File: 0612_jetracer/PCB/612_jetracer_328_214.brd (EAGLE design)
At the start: 86.7 x 51.7 mm, 90 parts, among them IC2 JETSON_NANO_NOBORDER, IC3 MULTIPLEXERSMC74HC157A, M1 MOSFET-N_FDN335N, M2 MOSFET-N_FDN335N, M3 MOSFET-N_FDN335N, M4 MOSFET-N_FDN335N, M5 MOSFET-N_FDN335N, M6 MOSFET-N_FDN335N, Q1 MOSFET-N_FDN335N, Q2 MOSFET-N_FDN335N, X2 16MHz

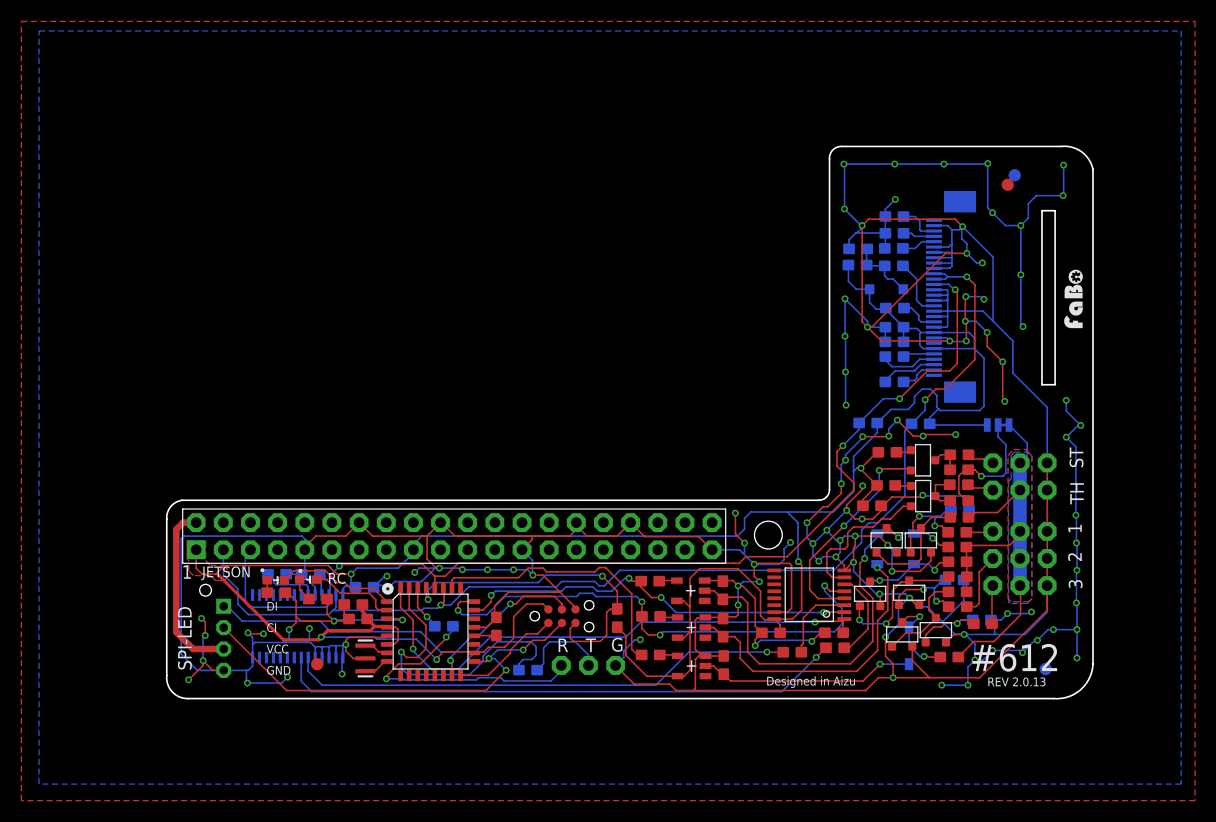
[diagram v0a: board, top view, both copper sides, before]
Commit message: #612 JetRacer ファイルリネーム,シルク追加位置修正、GNDビア追加
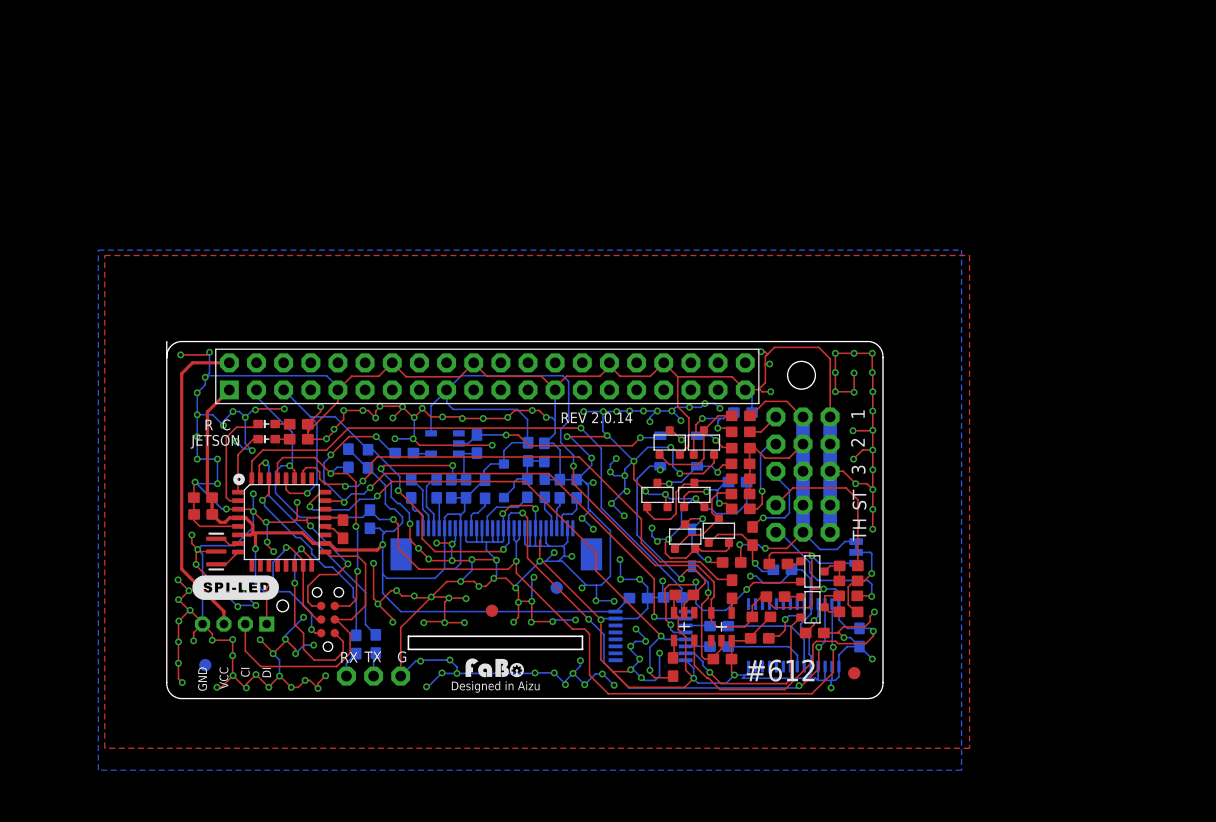
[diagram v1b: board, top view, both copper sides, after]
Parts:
- R15, R21, R26, R30, R4, R6: value 10K -> 1K
- moved U$2 88.5 mm to (3.60, 3.12), turned to 90 degrees
- moved U$24 65.6 mm to (30.8, 1.85), turned to 0 degrees
- moved R9 52.3 mm to (19.0, 16.8), turned to 90 degrees
- moved U$1 47.9 mm to (64.3, 2.38), turned to 270 degrees
- moved R1 47.5 mm to (60.6, 6.13), flipped to the top
- moved R7 46.9 mm to (18.8, 22.4), turned to 90 degrees
- moved C2 46.5 mm to (64.8, 5.71), turned to 90 degrees
- moved IC4 46.4 mm to (58.7, 5.92)
- moved U$3 46.4 mm to (36.5, 10.4)
- moved C5 46.3 mm to (22.9, 19.6), turned to 270 degrees
- moved U1 45.9 mm to (31.0, 16.2), turned to 0 degrees
- moved R3 45.5 mm to (55.5, 5.63), flipped to the top
- moved C4 44.6 mm to (25.2, 19.6), turned to 90 degrees
- moved C7 43.7 mm to (26.6, 19.6), turned to 270 degrees
- moved C6 42.8 mm to (28.0, 19.6), turned to 270 degrees
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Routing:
- net GND: track 673.8 -> 753.8 mm, vias 104 -> 210
- net N$43: track 53.4 -> 7.88 mm, vias 1 -> 0
- net N$42: track 47.5 -> 10.2 mm, vias 1 -> 0
- net CH3: track 25.7 -> 49.8 mm, vias 0 -> 2
- net N$6: track 26.2 -> 2.49 mm, vias 2 -> 0
- net AVR_MOSI: track 38.8 -> 16.5 mm
- net CH1: track 38.2 -> 55.4 mm, vias 4 -> 5
- net SDA: track 106.0 -> 91.0 mm, vias 3 -> 4
- net AVR_RX: track 4.27 -> 19.2 mm
- net N$34: track 33.5 -> 20.3 mm, vias 1 -> 2
- net 5V: track 16.8 -> 29.9 mm
- net N$10: track 2.60 -> 15.6 mm
- net AVR_SCK: track 41.4 -> 28.8 mm, vias 3 -> 0
- net N$14: track 2.98 -> 14.9 mm, vias 0 -> 1
- net SCL: track 98.8 -> 90.3 mm, vias 4 -> 7
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- removed copper zone on layer 1, net 3V3
- removed copper zone on layer 1, net VCC_RC
- removed copper zone on layer 16, net VCC_RC
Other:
- board size 86.7 x 51.7 mm -> 67 x 33.4 mm
- board text added: "F-612-2-14-A-N-J-0-P"
- board text added: "O"
- board text added: "R C"
- board text added: "REV 2.0.14"
- board text added: "X"
- board text added: "Y"
- board text removed: "1"
- board text removed: "F-612-2-13-A-N-J-0-P"
- board text removed: "R"
- board text removed: "REV 2.0.13"
- board text removed: "T"

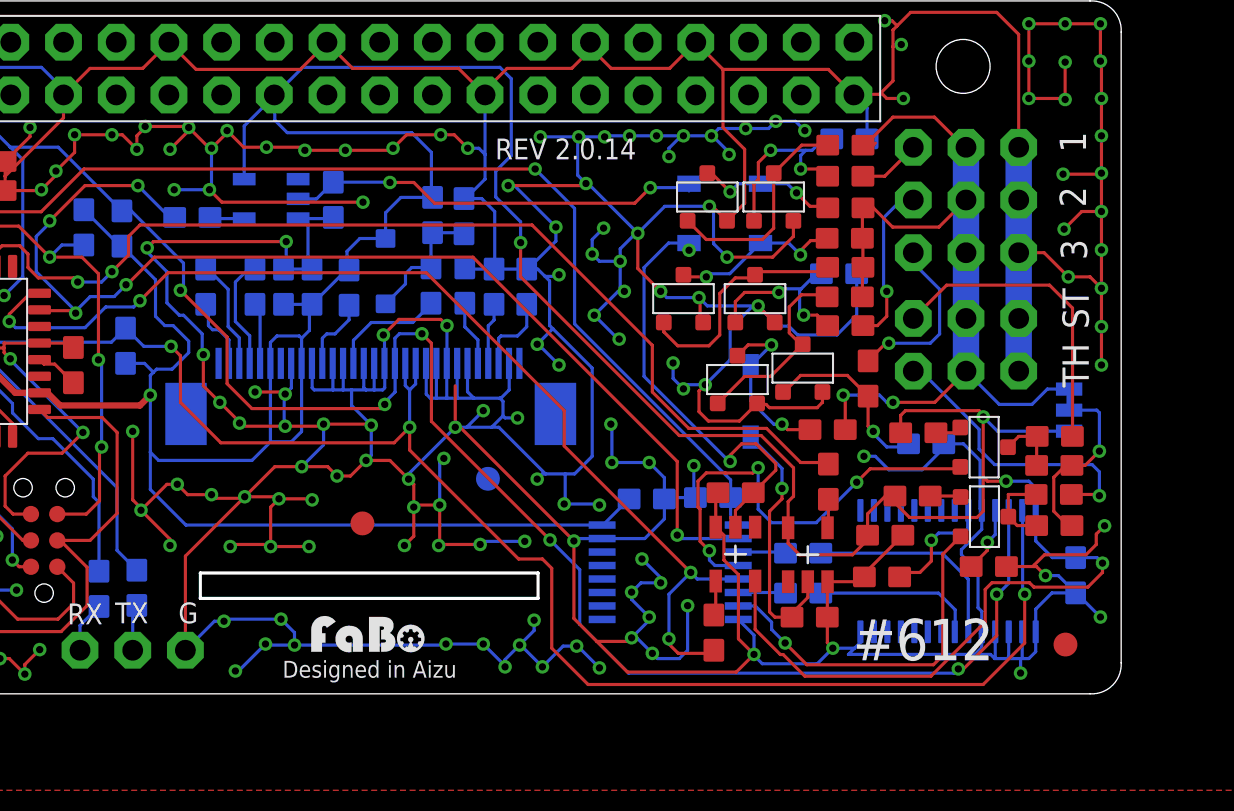
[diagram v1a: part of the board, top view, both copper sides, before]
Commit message: #612 JetRacer RCのみ操縦のため電源経路変更
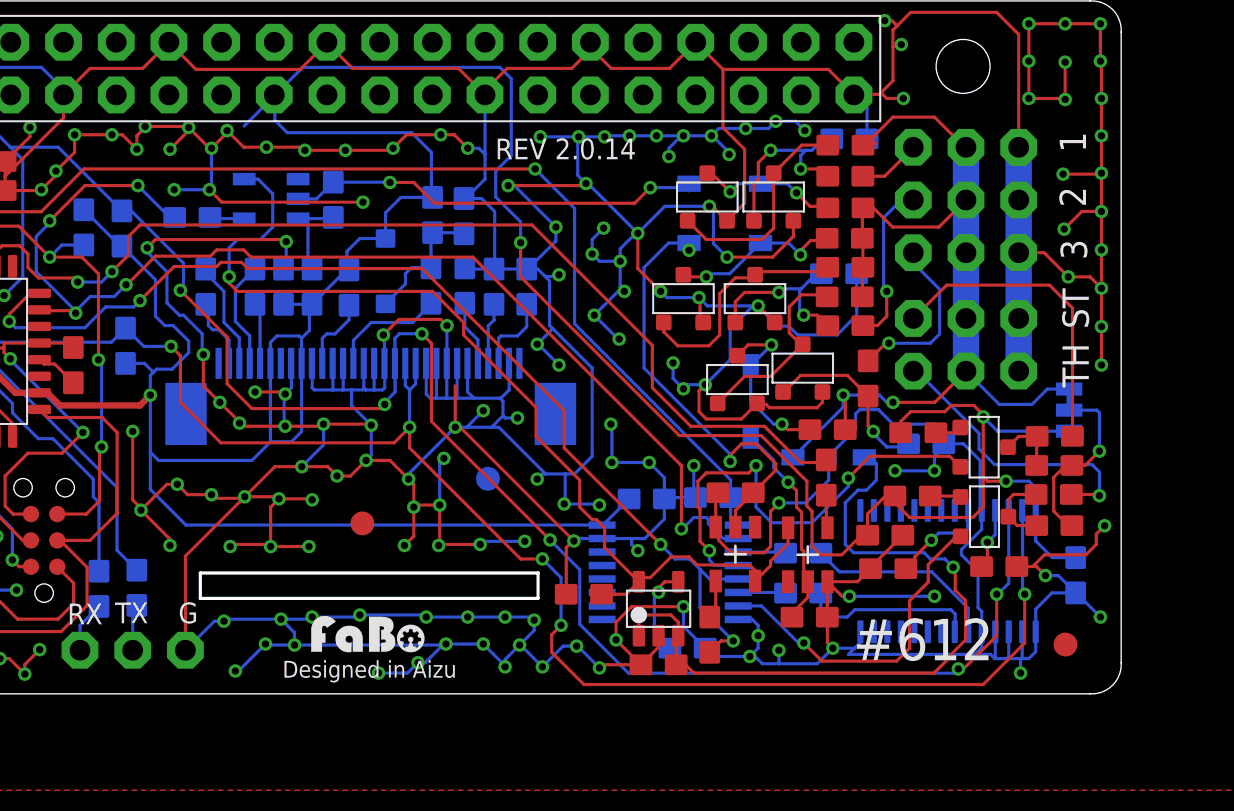
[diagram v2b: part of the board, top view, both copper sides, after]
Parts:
- added C10: 1uF, FaBo-Capacitor:0603
- added C22: 4.7uF, FaBo-Capacitor:0603
- added C23: 0.01uF, FaBo-Capacitor:0603
- added D5: 1N4148W, Diode:SOD3715X135
- added IC5: (no value), FaBo-Supply:SOT-23-5
- moved R3 0.50 mm to (55.8, 6.04)
- moved R1 0.50 mm to (61.1, 6.13)
- moved R25 0.22 mm to (47.2, 2.85)
- moved R32 0.22 mm to (52.8, 10.4)
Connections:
- new net N$47: C23.2, IC5.4
- new net N$48: C10.2, D5.1, IC5.1, IC5.3
- new net RC_3V3: C22.2, IC5.5, U$14.5, U$20.5, U$23.5
- net 3V3: no longer U$14.5, U$20.5, U$23.5
- net GND: now also C10.1, C22.1, C23.1, IC5.2
- net VCC_RC: now also D5.2
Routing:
- net RC_3V3: track 0.00 -> 47.9 mm, vias 0 -> 1
- net N$48: track 0.00 -> 34.7 mm, vias 0 -> 1
- net 3V3: track 239.7 -> 211.4 mm, vias 7 -> 6
- net GND: track 753.8 -> 777.2 mm, vias 210 -> 219
- net N$47: track 0.00 -> 4.37 mm, vias 0 -> 1
- net VCC_RC: track 42.7 -> 46.7 mm
- net N$37: track 12.5 -> 10.1 mm
- net RCH2: track 17.5 -> 16.1 mm
- net N$42: track 10.2 -> 9.34 mm
- net RCH1: track 21.8 -> 22.6 mm
- net CH1: track 55.4 -> 56.1 mm
- net N$43: track 7.88 -> 8.45 mm
- net CH2: track 52.2 -> 51.7 mm
- net N$7: track 5.73 -> 5.18 mm
- net SDA: track 91.0 -> 91.4 mm, vias 4 -> 6
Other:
- board text added: "#612 JetRacer Rev2.0.14"

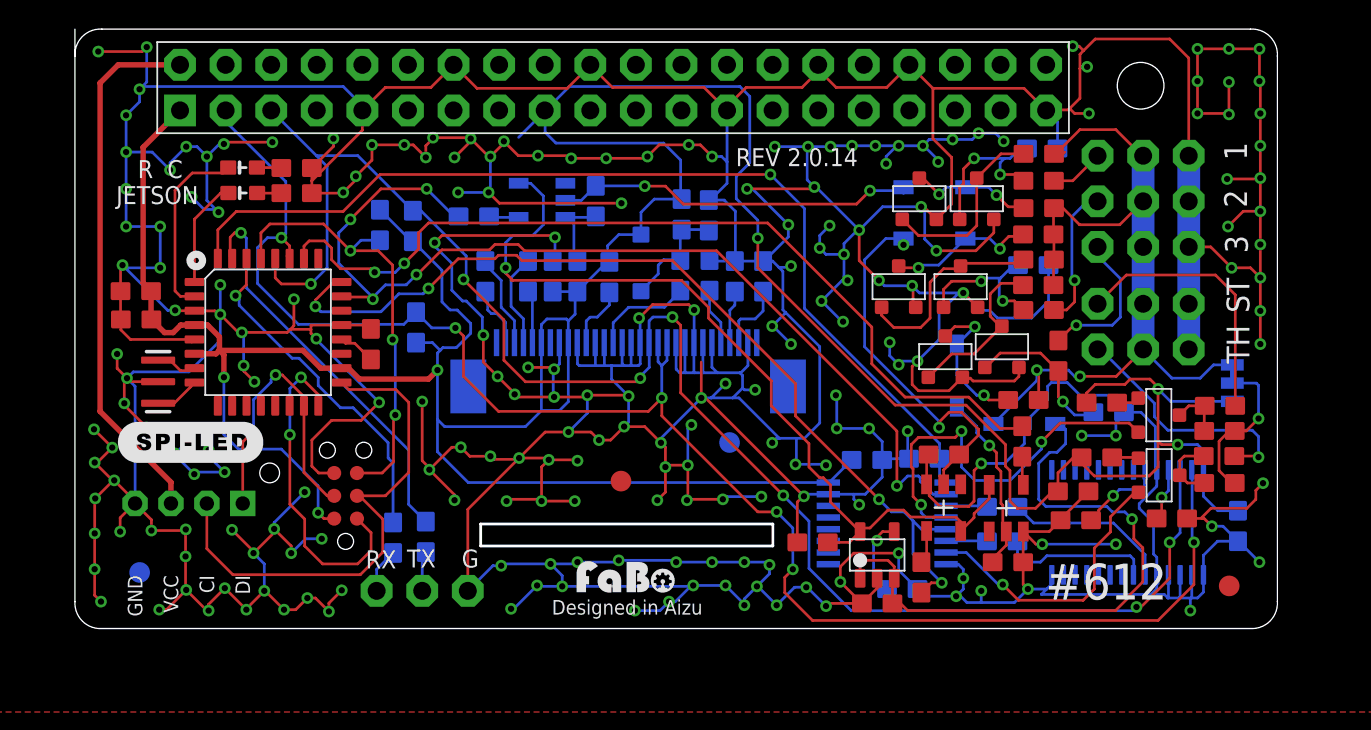
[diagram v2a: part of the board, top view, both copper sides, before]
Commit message: #612 JetRacer PCA9685 OEとボタンを追加
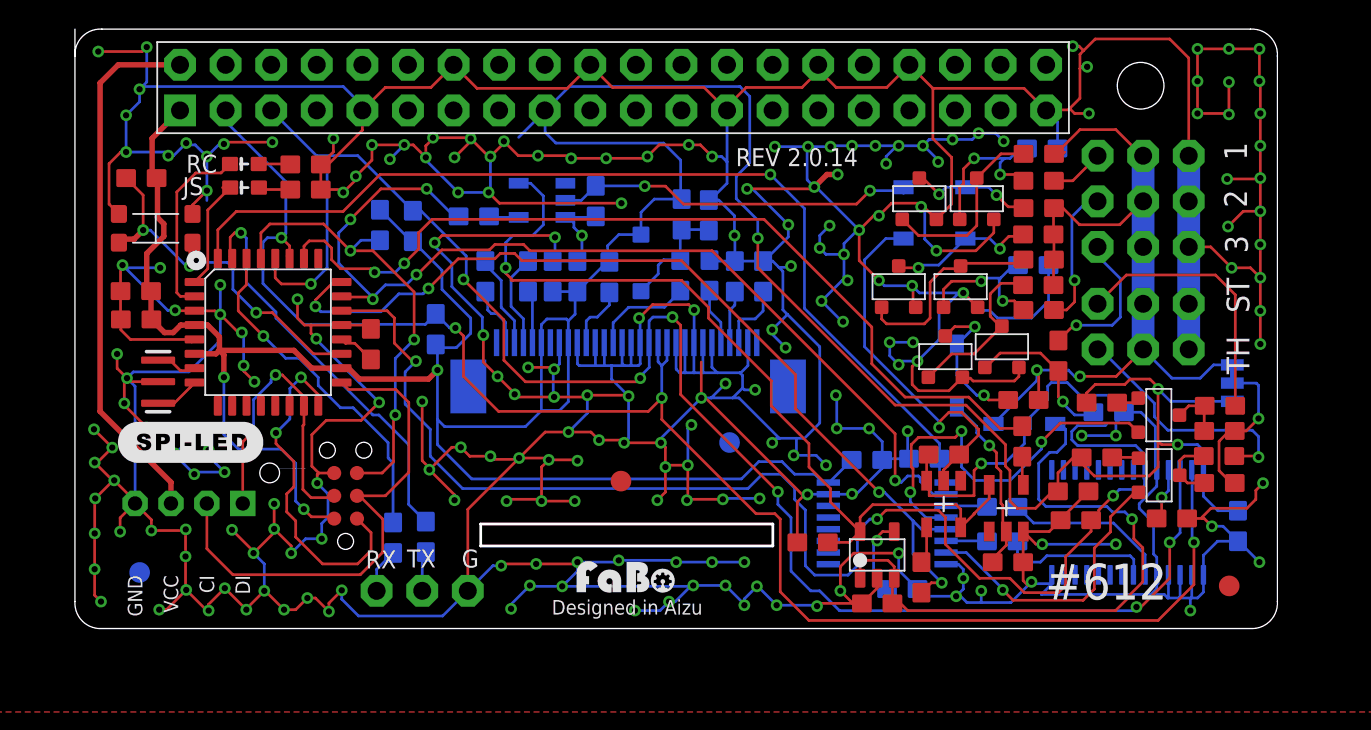
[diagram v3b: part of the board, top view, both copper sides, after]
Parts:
- added R41: DNP, FaBo-Resistors:0603
- added SW1: (no value), FaBo-Switch:KMR2
- added U$4: (no value), FaBo-Logo:LOGO_FABO_L_BOTTOM
- moved R9 1.10 mm to (20.1, 16.7)
- moved R10 0.54 mm to (12.8, 25.9)
- moved R5 0.54 mm to (12.8, 24.5)
- moved JETSON1 0.32 mm to (9.45, 24.6)
- moved JETSON 0.22 mm to (9.44, 25.9)
- moved U$20 0.20 mm to (48.4, 6.93)
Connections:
- new net OE_PIN: IC1.22, IC4.23, R3.2
- net 3V3: now also R41.2
- net GND: now also SW1.1, SW1.2
- net N$7: now also IC1.19, R41.1, SW1.3, SW1.4; no longer IC4.23, R3.2
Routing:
- net OE_PIN: track 0.00 -> 76.1 mm, vias 0 -> 3
- net N$7: track 5.18 -> 21.1 mm, vias 1 -> 3
- net GND: track 777.2 -> 780.7 mm, vias 219 -> 220
- net AVR_MISO: track 18.5 -> 19.5 mm
- net SDA: track 91.4 -> 90.7 mm, vias 6 -> 4
- net AVR_MOSI: track 16.5 -> 17.2 mm
- net SCL: track 90.3 -> 90.9 mm
- net AVR_RESET: track 25.2 -> 25.9 mm
- net RC_3V3: track 47.9 -> 48.6 mm
- net N$30: track 21.1 -> 20.5 mm, vias 2 -> 1
- net D3: track 6.00 -> 6.52 mm
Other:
- board text added: "JS"
- board text removed: "JETSON"
- board text removed: "R C"

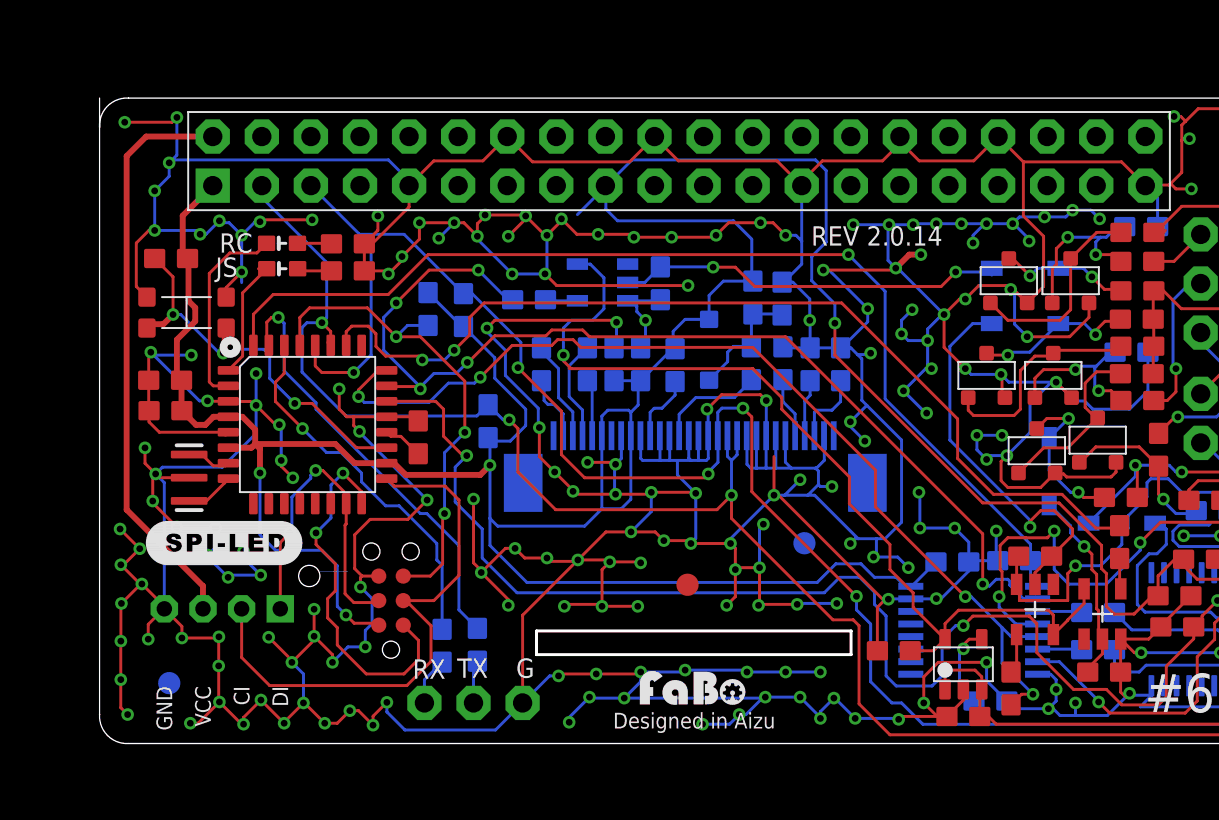
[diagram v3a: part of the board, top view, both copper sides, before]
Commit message: #612 JetRacer ロゴ変更裏、配線間隔修正
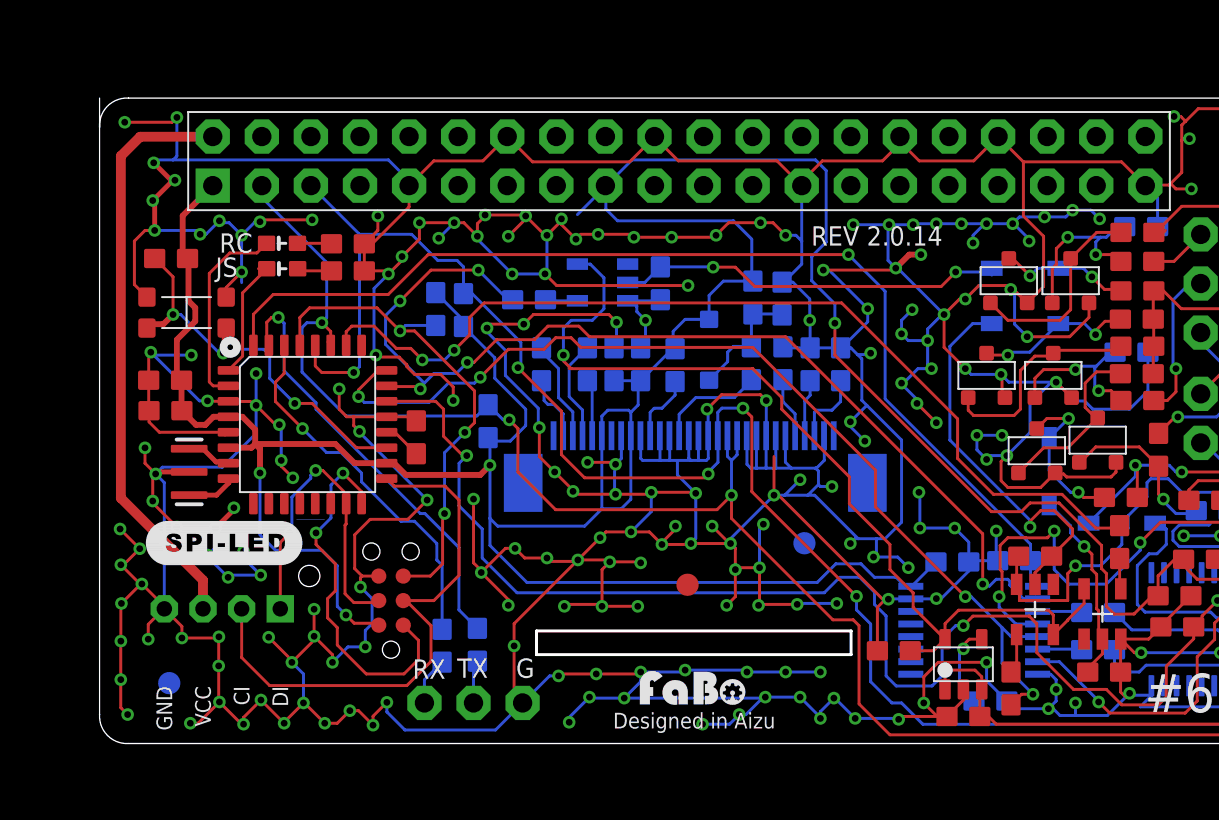
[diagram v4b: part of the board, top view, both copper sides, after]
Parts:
- moved U$4 2.95 mm to (9.30, 11.1)
- moved R2 0.40 mm to (17.4, 22.5)
- moved X2 0.30 mm to (4.63, 14.1)
- moved C1 0.10 mm to (16.4, 15.8)
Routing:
- net GND: track 780.7 -> 798.2 mm, vias 220 -> 231
- net N$15: track 2.33 -> 2.99 mm
